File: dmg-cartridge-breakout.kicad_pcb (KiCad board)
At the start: 2 copper layers, 51 x 61 mm, 2 parts, among them J1 Conn_01x32, J2 dmg-card

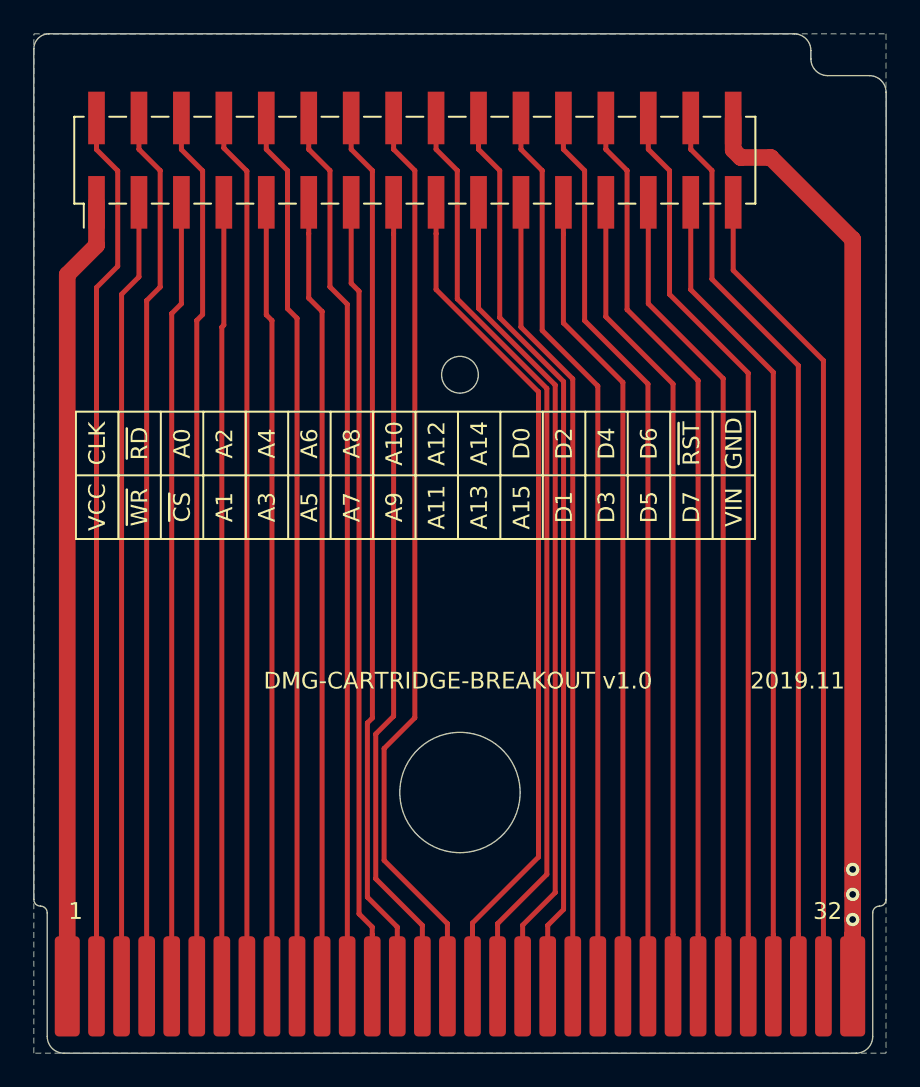
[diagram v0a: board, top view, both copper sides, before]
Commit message: remove B.Cu zone
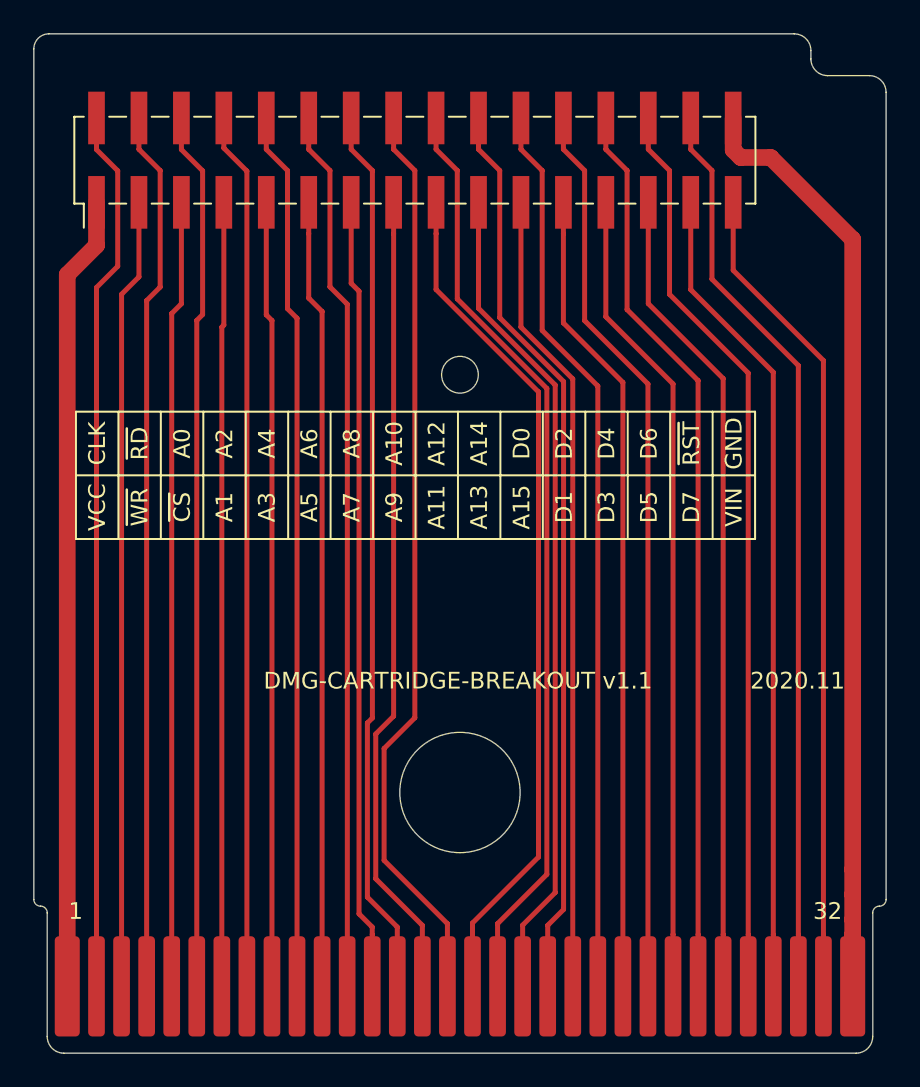
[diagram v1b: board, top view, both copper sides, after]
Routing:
- net Net-(J1-Pad32): vias 3 -> 0
- removed copper zone on B.Cu, net Net-(J1-Pad32)
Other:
- board text added: "2020.11"
- board text added: "DMG-CARTRIDGE-BREAKOUT v1.1"
- board text removed: "2019.11"
- board text removed: "DMG-CARTRIDGE-BREAKOUT v1.0"
